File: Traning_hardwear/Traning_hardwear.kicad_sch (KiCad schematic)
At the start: 0 parts

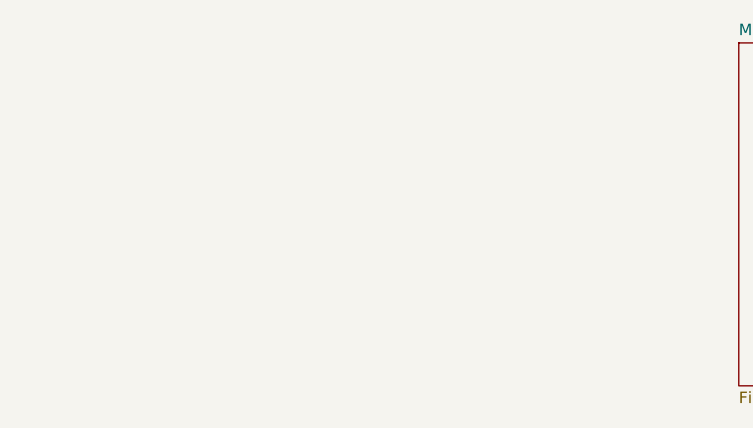
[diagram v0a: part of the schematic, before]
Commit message: add CAN
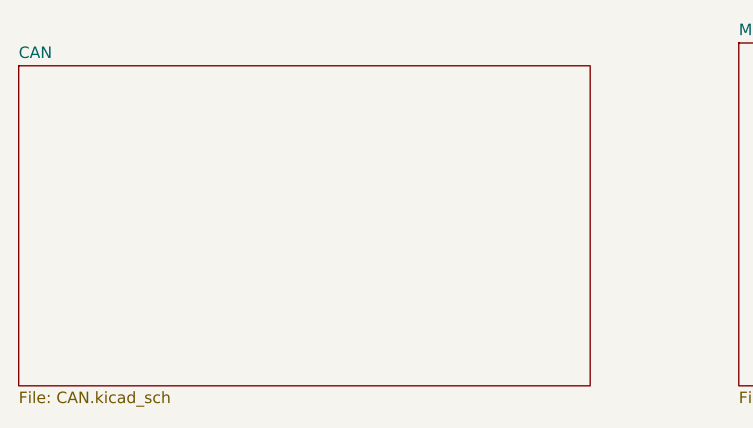
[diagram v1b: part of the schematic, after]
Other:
- added sheet CAN (CAN.kicad_sch)
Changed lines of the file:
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@@
+		)
+	)
+	(sheet
+		(at 25.4 96.52)
+		(size 63.5 35.56)
+		(exclude_from_sim no)
+		(in_bom yes)
+		(on_board yes)
+		(dnp no)
+		(fields_autoplaced yes)
+		(stroke
+			(width 0.1524)
+			(type solid)
+		)
+		(fill
+			(color 0 0 0 0.0000)
+		)
+		(property "Sheetname" "CAN"
+			(at 25.4 95.8084 0)
+			(effects
+				(font
+					(size 1.27 1.27)
+				)
+				(justify left bottom)
+			)
+		)
+		(property "Sheetfile" "CAN.kicad_sch"
+			(at 25.4 132.6646 0)
+			(effects
+				(font
+					(size 1.27 1.27)
+				)
+				(justify left top)
+			)
+		)
+		(instances
+			(project "Traning_hardwear"
+				(path "/30fb269d-181e-4844-9e82-e5c3e09101dc"
+					(page "4")
+				)
+			)
 		)
 	)

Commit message: Finish Schematic
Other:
- sheet CAN ports: added RXD, STBY, TXD; removed none
- sheet MCU ports: added CRX1, CTX1, STBY; removed none
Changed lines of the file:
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@@
 	(generator_version "9.0")
 	(paper "A4")
+	(wire
+		(pts
+			(xy 88.9 102.87) (xy 105.41 102.87)
+		)
+		(stroke
+			(width 0)
+			(type default)
+		)
+	)
+	(wire
+		(pts
+			(xy 88.9 113.03) (xy 105.41 113.03)
+		)
+		(stroke
+			(width 0)
+			(type default)
+		)
+	)
+	(wire
+		(pts
+			(xy 88.9 125.73) (xy 88.9 124.46)
+		)
+		(stroke
+			(width 0)
+			(type default)
+		)
+	)
+	(wire
+		(pts
+			(xy 105.41 125.73) (xy 88.9 125.73)
+		)
+		(stroke
+			(width 0)
+			(type default)
+		)
+	)
 	(sheet
 		(at 186.69 95.25)
@@
 			)
 		)
+		(pin "CRX1" input
+			(at 105.41 102.87 180)
+			(effects
+				(font
+					(size 1.27 1.27)
+				)
+				(justify left)
+			)
+		)
+		(pin "CTX1" output
+			(at 105.41 125.73 180)
+			(effects
+				(font
+					(size 1.27 1.27)
+				)
+				(justify left)
+			)
+		)
+		(pin "STBY" output
+			(at 105.41 113.03 180)
+			(effects
+				(font
+					(size 1.27 1.27)
+				)
+				(justify left)
+			)
+		)
 		(instances
 			(project "Traning_hardwear"
@@
 			)
 		)
+		(pin "RXD" output
+			(at 88.9 102.87 0)
+			(effects
+				(font
+					(size 1.27 1.27)
+				)
+				(justify right)
+			)
+		)
+		(pin "STBY" input
+			(at 88.9 113.03 0)
+			(effects
+				(font
+					(size 1.27 1.27)
+				)
+				(justify right)
+			)
+		)
+		(pin "TXD" input
+			(at 88.9 124.46 0)
+			(effects
+				(font
+					(size 1.27 1.27)
+				)
+				(justify right)
+			)
+		)
